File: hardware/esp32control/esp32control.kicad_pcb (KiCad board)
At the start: 2 copper layers, 67.6 x 85.9 mm, 74 parts, among them J1 Conn_02x07_Odd_Even, P1 CONN_01X05, Q1 BSS138, Q2 BSS138, Q3 BSS138, Q4 BSS138, Q5 BSS138, Q6 BSS138, SW1 Boot, SW2 Reset, U1 ESP32-WROOM, U10 LTV-354T, U11 HUT4, U12 LM1117-3.3, U2 AQY212, U3 AQY212, U4 LM2675M-5, U5 LTV-354T, U6 AQY212, U7 AQY212, U8 LTV-354T, U9 LTV-354T

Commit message: pcb update
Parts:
- removed C1: 100n, Capacitors_SMD:C_0603
- removed P1: CONN_01X05, Pin_Headers:Pin_Header_Straight_1x05_Pitch2.54mm
- added Q7: MMBT3904, Package_TO_SOT_SMD:SOT-23, F.Cu at (101.1, 87.5)
- added Q8: MMBT3904, Package_TO_SOT_SMD:SOT-23, F.Cu at (105.9, 87.5)
- added R20: 10k, Resistors_SMD:R_0603, F.Cu at (106.1, 90.3)
- added R21: 10k, Resistors_SMD:R_0603, F.Cu at (103.3, 90.3)
- C23: value 100n -> 1u
- J1: value Conn_02x07_Odd_Even -> Conn_02x09_Odd_Even; footprint Pin_Headers:Pin_Header_Straight_2x07_Pitch2.54mm -> Pin_Headers:Pin_Header_Straight_2x09_Pitch2.54mm
- R1, R24, R26, R6: value 10k -> 1k
- R2, R25, R27, R7: value 470 -> 1k
- R3, R4, R5, R8: value 10k -> 1k5
- moved J1 4.19 mm to (110.7, 67.4)
- turned R1 to 270 degrees
- turned R2 to 90 degrees
- turned R24 to 270 degrees
- turned R25 to 90 degrees
- turned R26 to 270 degrees
- turned R27 to 90 degrees
- turned R6 to 270 degrees
- turned R7 to 90 degrees
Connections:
- J1 pad 10: /IO5 -> /IO25
- J1 pad 11: /SCL -> /IO26
- J1 pad 12: /SDA -> /IO27
- J1 pad 13: GND -> /IO4
- J1 pad 14: GND -> /IO5
- J1 pad 2: /IO36 -> /TXD0
- J1 pad 3: /IO39 -> /RXD0
- J1 pad 4: /IO32 -> /RTS
- J1 pad 5: /IO33 -> /DTS
- J1 pad 6: /IO25 -> /IO36
- J1 pad 7: /IO26 -> /IO39
- J1 pad 8: /IO27 -> /IO32
- J1 pad 9: /IO4 -> /IO33
- R1 pad 1: Net-(R1-Pad1) -> Net-(Q1-Pad3)
- R1 pad 2: +3V3 -> Net-(R1-Pad2)
- R17 pad 1: /OPTO1 -> /IO33
- R19 pad 2: Net-(R19-Pad2) -> /nReset
- R2 pad 1: Net-(Q1-Pad3) -> Net-(D1-Pad1)
- R2 pad 2: Net-(D1-Pad1) -> Net-(Q1-Pad3)
- R24 pad 1: Net-(R24-Pad1) -> Net-(Q3-Pad3)
- R24 pad 2: +3V3 -> Net-(R24-Pad2)
- R25 pad 1: Net-(Q3-Pad3) -> Net-(D9-Pad1)
- R25 pad 2: Net-(D9-Pad1) -> Net-(Q3-Pad3)
- R26 pad 1: Net-(R26-Pad1) -> Net-(Q4-Pad3)
- R26 pad 2: +3V3 -> Net-(R26-Pad2)
- R27 pad 1: Net-(Q4-Pad3) -> Net-(D11-Pad1)
- R27 pad 2: Net-(D11-Pad1) -> Net-(Q4-Pad3)
- R30 pad 1: /OPTO2 -> /IO32
- R6 pad 1: Net-(R6-Pad1) -> Net-(Q2-Pad3)
- R6 pad 2: +3V3 -> Net-(R6-Pad2)
- R7 pad 1: Net-(Q2-Pad3) -> Net-(D3-Pad1)
- R7 pad 2: Net-(D3-Pad1) -> Net-(Q2-Pad3)
- U1 pad 13: /OPTO2 -> Net-(U1-Pad13)
- U1 pad 14: /OPTO1 -> Net-(U1-Pad14)
- U1 pad 3: Net-(R19-Pad2) -> /nReset
- U1 pad 34: Net-(P1-Pad2) -> /RXD0
- U1 pad 35: Net-(P1-Pad1) -> /TXD0
- U2 pad 1: Net-(R1-Pad1) -> +3V3
- U2 pad 2: /CH1 -> Net-(R1-Pad2)
- U3 pad 1: Net-(R6-Pad1) -> +3V3
- U3 pad 2: /CH2 -> Net-(R6-Pad2)
- U5 pad 4: /OPTO1 -> /IO33
- U6 pad 1: Net-(R24-Pad1) -> +3V3
- U6 pad 2: /CH3 -> Net-(R24-Pad2)
- U7 pad 1: Net-(R26-Pad1) -> +3V3
- U7 pad 2: /CH4 -> Net-(R26-Pad2)
- U8 pad 4: /OPTO2 -> /IO32
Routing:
- net /SDA: track 69.3 -> 14.1 mm
- net /SCL: track 56.9 -> 5.93 mm
- net /IO5: track 34.9 -> 3.33 mm
- net /IO4: track 36.1 -> 7.89 mm
- net +3V3: track 205.1 -> 177.6 mm
- net GND: track 247.5 -> 221.6 mm, vias 54 -> 47
- net /CH4: track 30.8 -> 5.19 mm
- net Net-(P1-Pad2): track 20.5 -> 0.00 mm
- net /RXD0: track 0.00 -> 20.5 mm
- net Net-(P1-Pad1): track 18.2 -> 0.00 mm
- net /TXD0: track 0.00 -> 18.2 mm
- net /+5V: track 121.2 -> 106.0 mm
- net /nReset: track 67.5 -> 81.4 mm, vias 1 -> 4
- net /IO36: track 31.7 -> 20.5 mm
- net /IO39: track 27.9 -> 18.3 mm
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
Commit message: updated sch & pcb
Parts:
- J1: value Conn_02x09_Odd_Even -> Conn_02x10_Odd_Even; footprint Pin_Headers:Pin_Header_Straight_2x09_Pitch2.54mm -> Pin_Headers:Pin_Header_Straight_2x10_Pitch2.54mm
- moved R27 1.70 mm to (115.3, 94.1), turned to 180 degrees
- moved J1 1.30 mm to (112.0, 67.7)
- moved Q4 1.10 mm to (107.2, 93.3)
- moved R26 0.80 mm to (112.0, 94.1), turned to 180 degrees
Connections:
- J1 pad 13: /IO4 -> /SCL
- J1 pad 14: /IO5 -> /SDA
- J1 pad 15: /SCL -> /CH1
- J1 pad 16: /SDA -> /CH2
- J1 pad 17: GND -> /CH3
- J1 pad 18: GND -> /CH4
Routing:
- net /SDA: track 14.1 -> 67.7 mm, vias 2 -> 3
- net /SCL: track 5.93 -> 55.0 mm
- net /CH1: track 10.7 -> 47.3 mm, vias 0 -> 3
- net /CH4: track 5.19 -> 38.9 mm
- net /CH2: track 11.2 -> 43.3 mm, vias 0 -> 1
- net /RTS: track 0.25 -> 29.7 mm, vias 0 -> 1
- net /TXD0: track 18.2 -> 38.7 mm, vias 0 -> 1
- net /CH3: track 20.8 -> 37.9 mm, vias 0 -> 1
- net /RXD0: track 20.5 -> 35.6 mm, vias 0 -> 1
- net /+5V: track 106.0 -> 119.5 mm
- net /IO32: track 34.6 -> 47.3 mm
- net /IO36: track 20.5 -> 30.8 mm
- net /IO39: track 18.3 -> 28.2 mm, vias 1 -> 2
- net /nReset: track 81.4 -> 90.8 mm, vias 4 -> 7
- net /IO27: track 37.0 -> 45.8 mm
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
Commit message: pcb update
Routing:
- net GND: track 222.5 -> 226.0 mm, vias 51 -> 46
- net /CH4: track 38.9 -> 37.7 mm
- net /SDA_EXT: track 13.0 -> 13.3 mm, vias 0 -> 2

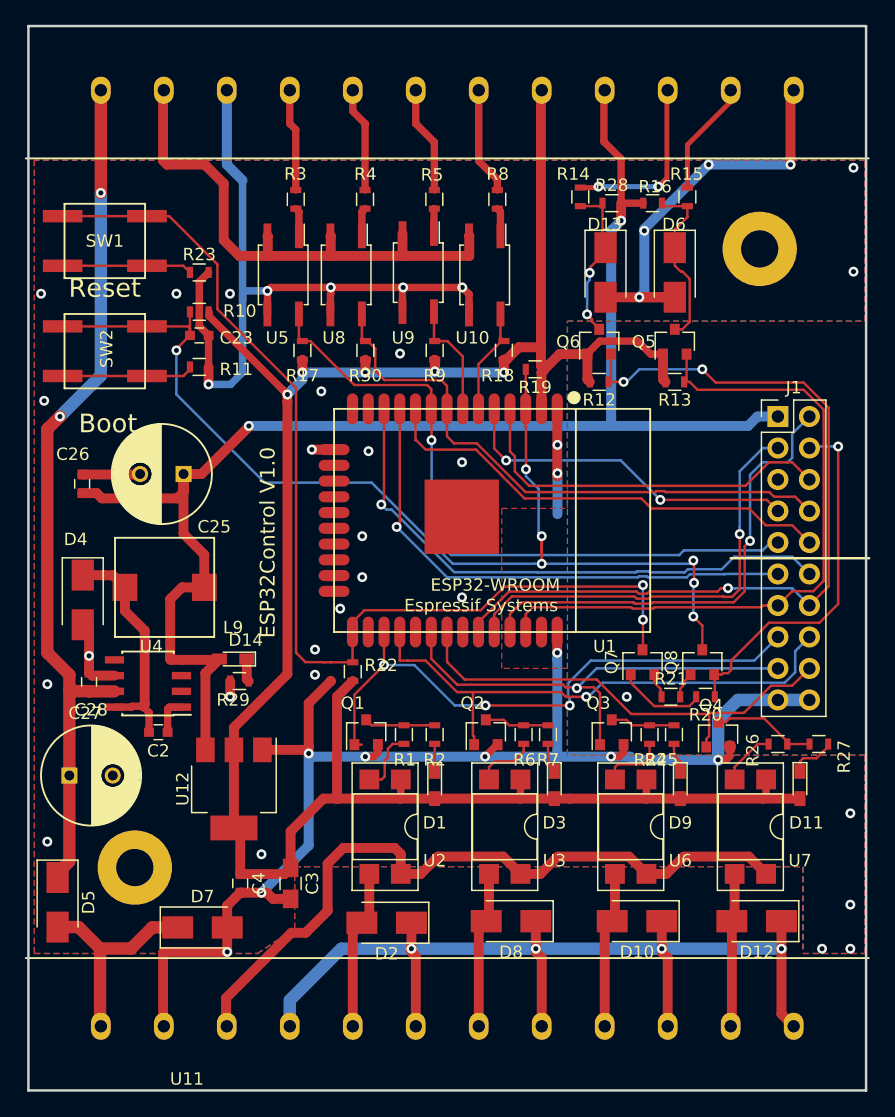
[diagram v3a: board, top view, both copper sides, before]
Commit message: update libs to kicad 5.1.5
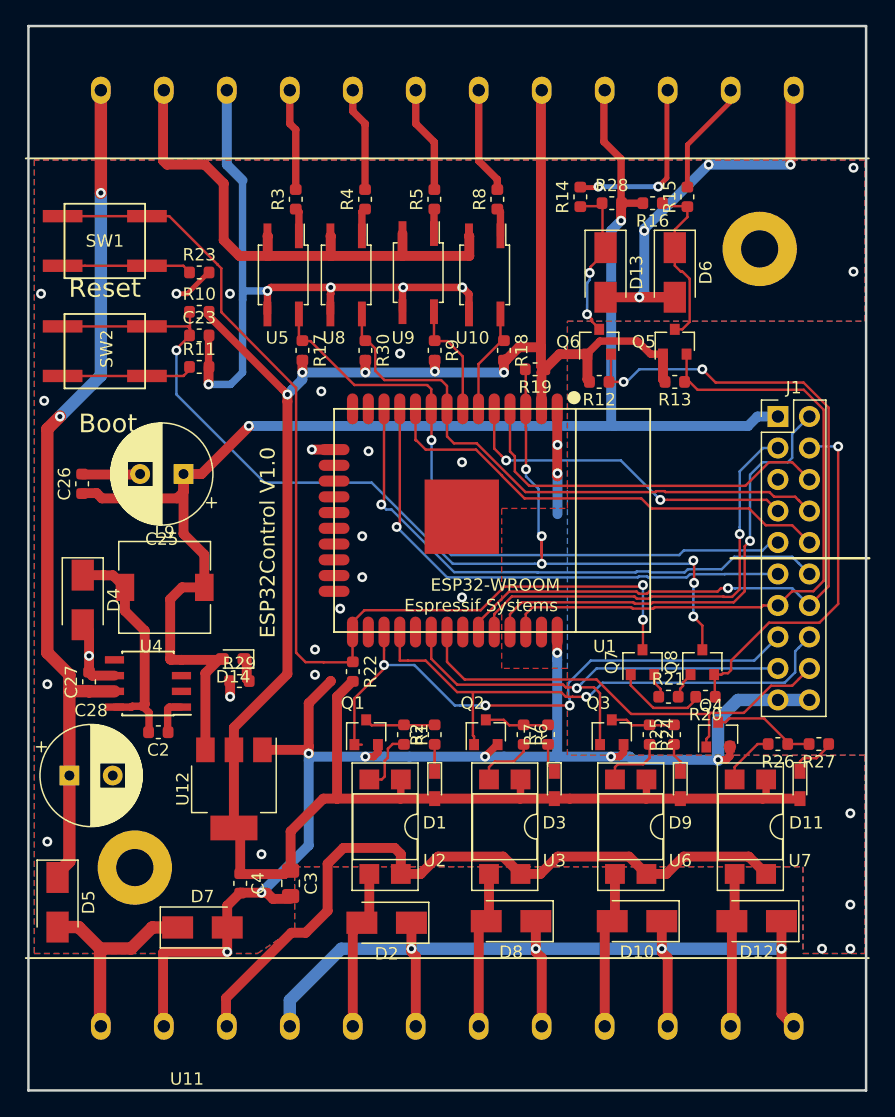
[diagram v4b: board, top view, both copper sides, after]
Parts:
- C2, C23, C26, C27, C4: footprint Capacitors_SMD:C_0603 -> Capacitor_SMD:C_0603_1608Metric
- C25, C28: footprint Capacitors_ThroughHole:C_Radial_D8_L11.5_P3.5 -> Capacitor_THT:CP_Radial_D8.0mm_P3.50mm
- C3: footprint Capacitors_SMD:C_0805_HandSoldering -> Capacitor_SMD:C_0805_2012Metric_Pad1.15x1.40mm_HandSolder
- D10, D12, D13, D2, D4, D5, D6, D7, D8: footprint Diodes_SMD:D_SMA -> Diode_SMD:D_SMA
- D14: footprint LEDs:LED_0603_HandSoldering -> LED_SMD:LED_0603_1608Metric_Pad1.05x0.95mm_HandSolder
- J1: footprint Pin_Headers:Pin_Header_Straight_2x10_Pitch2.54mm -> Connector_PinHeader_2.54mm:PinHeader_2x10_P2.54mm_Vertical
- L9: footprint smd_packages:WE-PD-7345 -> Inductor_SMD:L_7.3x7.3_H4.5
- R1, R10, R11, R12, R13, R14, R15, R16, R17, R18, R19, R2, R20, R21, R22, R23, R24, R25, R26, R27, R28, R29, R3, R30, R4, R5, R6, R7, R8, R9: footprint Resistors_SMD:R_0603 -> Resistor_SMD:R_0603_1608Metric
- moved R21 0.19 mm to (103.2, 90.3)
- turned L9 to 0 degrees
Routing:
- net GND: track 226.0 -> 223.6 mm, vias 46 -> 45

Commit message: silk update, fab files regen, pdf added
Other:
- board text added: "ESP32Control V1.1"
- board text removed: "ESP32Control V1.0"

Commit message: revB initial
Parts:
- removed C25: CP_Small, Capacitor_THT:CP_Radial_D8.0mm_P3.50mm
- added BT1: Battery_Cell, Battery:BatteryHolder_Keystone_3001_1x12mm, F.Cu at (59.0, 67.5)
- added C1: 1u, Capacitor_SMD:C_0603_1608Metric, F.Cu at (63.0, 76.0)
- added C5: 47u 10V, Capacitor_SMD:C_1206_3216Metric, F.Cu at (66.2, 79.2)
- added C6: 47u 10V, Capacitor_SMD:C_1206_3216Metric, F.Cu at (70.8, 66.9)
- added D15: LED, LED_SMD:LED_0603_1608Metric_Pad1.05x0.95mm_HandSolder, F.Cu at (109.6, 62.2)
- added D16: LED, LED_SMD:LED_0603_1608Metric_Pad1.05x0.95mm_HandSolder, F.Cu at (114.3, 62.2)
- added R31: 100, Resistor_SMD:R_0603_1608Metric, F.Cu at (71.5, 72.0)
- added R32: 1k, Resistor_SMD:R_0603_1608Metric, F.Cu at (112.1, 62.0)
- added R33: 1k, Resistor_SMD:R_0603_1608Metric, F.Cu at (116.6, 62.0)
- added TP1: TestPoint, TestPoint:TestPoint_Pad_D1.5mm, F.Cu at (70.0, 78.0)
- added U13: RV-8523-C3, Package_SON:RTC_SMD_MicroCrystal_C3_2.5x3.7mm, F.Cu at (67.0, 75.0)
- moved R10 16.9 mm to (71.5, 75.0)
- moved R29 14.1 mm to (59.8, 78.0)
- moved C2 11.1 mm to (70.0, 85.5), turned to 270 degrees
- moved SW2 10.4 mm to (63.0, 53.5), turned to 90 degrees
- moved D14 9.93 mm to (62.5, 79.0), turned to 270 degrees
- moved C23 9.59 mm to (69.0, 70.0), turned to 180 degrees
- moved R23 9.07 mm to (70.5, 63.5)
- moved C27 8.66 mm to (65.0, 90.2), turned to 180 degrees
- moved D4 8.03 mm to (58.5, 90.1), turned to 0 degrees
- moved U4 5.97 mm to (65.2, 84.8), turned to 270 degrees
- moved R11 5.46 mm to (70.5, 62.0)
- moved L9 5.43 mm to (57.5, 83.5), turned to 90 degrees
- moved C26 4.88 mm to (55.8, 78.0), turned to 0 degrees
- moved U12 4.66 mm to (72.5, 99.2), turned to 0 degrees
- moved SW1 1.69 mm to (56.0, 53.5), turned to 90 degrees
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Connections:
- net /+5V renamed +5V
- net /GNDA renamed GNDA
- J1 pad 5: /DTS -> /DTR
- U1 pad 13: Net-(U1-Pad13) -> (no net)
- U1 pad 14: Net-(U1-Pad14) -> (no net)
- U1 pad 16: Net-(U1-Pad16) -> (no net)
- U1 pad 17: Net-(U1-Pad17) -> (no net)
- U1 pad 18: Net-(U1-Pad18) -> (no net)
- U1 pad 19: Net-(U1-Pad19) -> (no net)
- U1 pad 20: Net-(U1-Pad20) -> (no net)
- U1 pad 21: Net-(U1-Pad21) -> (no net)
- U1 pad 22: Net-(U1-Pad22) -> (no net)
- U1 pad 23: Net-(U1-Pad23) -> (no net)
- U1 pad 24: Net-(U1-Pad24) -> (no net)
- U1 pad 29: /IO5 -> (no net)
- U1 pad 32: Net-(U1-Pad32) -> (no net)
- U1 pad 37: Net-(U1-Pad37) -> /IO23
- U4 pad 2: Net-(U4-Pad2) -> (no net)
- U4 pad 3: Net-(U4-Pad3) -> (no net)
- U4 pad 5: Net-(U4-Pad5) -> (no net)
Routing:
- net +5V: track 119.5 -> 73.0 mm
- net GND: track 223.6 -> 186.0 mm, vias 45 -> 38
- net +3V3: track 183.9 -> 149.8 mm
- net /nReset: track 90.8 -> 62.6 mm, vias 7 -> 6
- net +24V: track 70.1 -> 42.4 mm
- net /nBoot: track 86.1 -> 59.4 mm
- net /DTR: track 2.04 -> 26.8 mm, vias 0 -> 3
- net Net-(C2-Pad2): track 18.7 -> 0.00 mm
- net Net-(R11-Pad1): track 10.7 -> 0.00 mm
- net Net-(R23-Pad1): track 10.5 -> 0.00 mm
- net /IO33: track 55.1 -> 50.1 mm
- net Net-(C2-Pad1): track 3.06 -> 1.17 mm
- net Net-(D14-Pad1): track 1.84 -> 0.00 mm
- added copper zone on F.Cu, net +5V

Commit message: pcb update, fab generated
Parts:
- moved C2 1.06 mm to (69.2, 84.8)
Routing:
- net +5V: track 73.0 -> 121.7 mm, vias 2 -> 7
- net +24V: track 42.4 -> 86.0 mm
- net +3V3: track 149.8 -> 183.8 mm, vias 5 -> 8
- net /nBoot: track 59.4 -> 92.1 mm, vias 2 -> 4
- net /nReset: track 62.6 -> 95.2 mm, vias 6 -> 7
- net /IO23: track 0.00 -> 30.6 mm, vias 0 -> 2
- net /SCL: track 55.0 -> 83.8 mm, vias 0 -> 2
- net Net-(R23-Pad1): track 0.00 -> 26.1 mm, vias 0 -> 2
- net /SDA: track 67.7 -> 92.4 mm, vias 3 -> 5
- net Net-(BT1-Pad1): track 0.00 -> 23.4 mm, vias 0 -> 1
- net /IO27: track 45.8 -> 68.5 mm, vias 1 -> 4
- net /IO4: track 0.00 -> 19.7 mm, vias 0 -> 2
- net /IO26: track 42.2 -> 61.9 mm, vias 1 -> 4
- net GND: track 186.0 -> 203.7 mm, vias 38 -> 39
- net Net-(R11-Pad1): track 0.00 -> 14.7 mm
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- added copper zone on F.Cu, net Net-(C2-Pad2)
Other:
- rule trace_min: 0.15 -> 0.2
- board text added: "ESP32Control RevB"
- board text removed: "ESP32Control V1.1"
